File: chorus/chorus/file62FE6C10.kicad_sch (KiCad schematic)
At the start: 7 parts, among them U10 MN3102

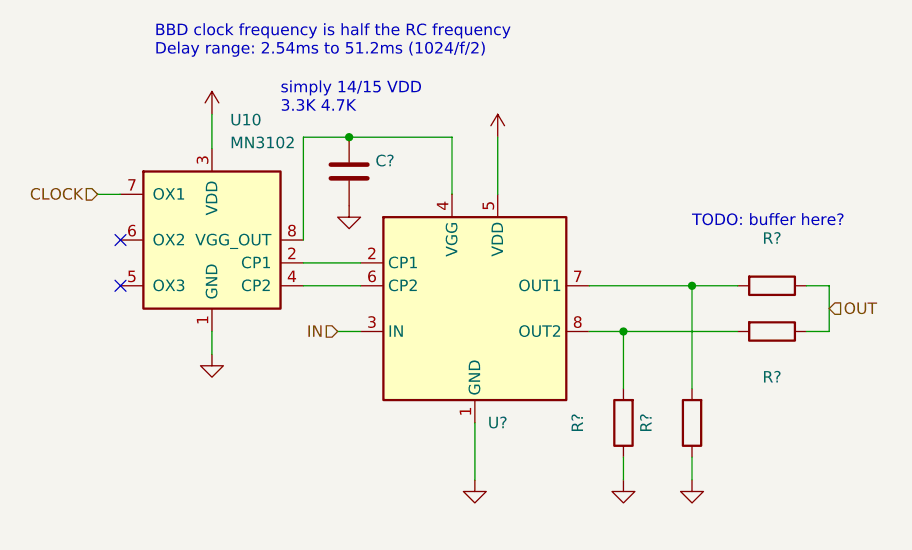
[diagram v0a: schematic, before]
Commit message: add output buffer
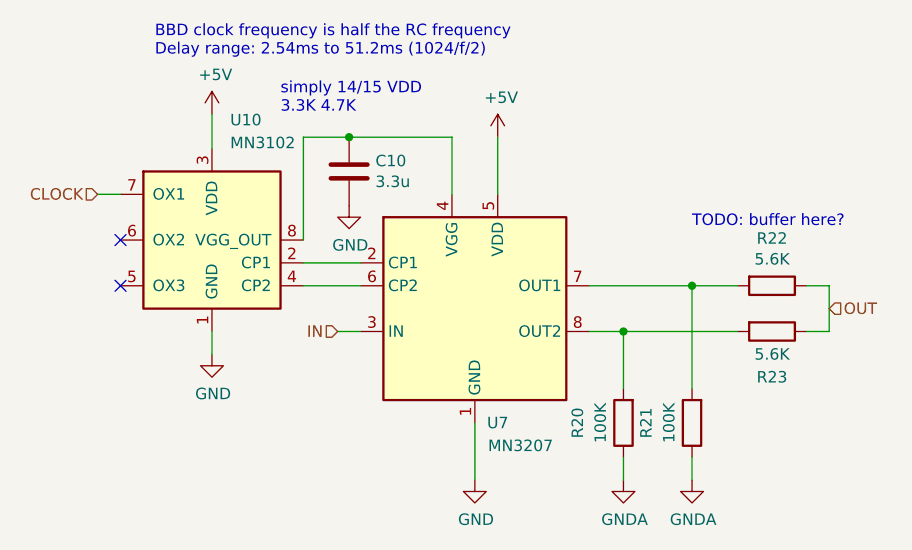
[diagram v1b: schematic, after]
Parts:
- C10: renamed from C?; value (none) -> 3.3u
- R20, R21: renamed from R?; value (none) -> 100K
- R22, R23: renamed from R?; value (none) -> 5.6K
- U7: renamed from U?; value (none) -> MN3207
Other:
- company: (none) -> rabidaudio
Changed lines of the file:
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@@
 (kicad_sch (version 20211123) (generator eeschema)
   (paper "A4")
+  (title_block
+    (company "rabidaudio")
+  )
   (junction (at 167.64 86.36) (diameter 0) (color 0 0 0 0)
   )
@@
   (symbol (lib_id "power:+5V") (at 114.3 67.31 0) (unit 1)
     (in_bom yes) (on_board yes)
-    (property "Reference" "#PWR?" (id 0) (at 114.3 71.12 0)
-      (effects (font (size 1.27 1.27)) hide)
-    )
-    (property "Value" "" (id 1) (at 114.681 62.9158 0))
+    (property "Reference" "#PWR04" (id 0) (at 114.3 71.12 0)
+      (effects (font (size 1.27 1.27)) hide)
+    )
+    (property "Value" "+5V" (id 1) (at 114.681 62.9158 0))
     (property "Footprint" "" (id 2) (at 114.3 67.31 0)
       (effects (font (size 1.27 1.27)) hide)
@@
   (symbol (lib_id "power:+5V") (at 146.05 69.85 0) (unit 1)
     (in_bom yes) (on_board yes)
-    (property "Reference" "#PWR?" (id 0) (at 146.05 73.66 0)
-      (effects (font (size 1.27 1.27)) hide)
-    )
-    (property "Value" "" (id 1) (at 146.431 65.4558 0))
+    (property "Reference" "#PWR05" (id 0) (at 146.05 73.66 0)
+      (effects (font (size 1.27 1.27)) hide)
+    )
+    (property "Value" "+5V" (id 1) (at 146.431 65.4558 0))
     (property "Footprint" "" (id 2) (at 146.05 69.85 0)
       (effects (font (size 1.27 1.27)) hide)
@@
   (symbol (lib_id "Device:R") (at 176.53 91.44 270) (unit 1)
     (in_bom yes) (on_board yes)
-    (property "Reference" "R?" (id 0) (at 176.53 96.52 90))
-    (property "Value" "" (id 1) (at 176.53 93.98 90))
+    (property "Reference" "R23" (id 0) (at 176.53 96.52 90))
+    (property "Value" "5.6K" (id 1) (at 176.53 93.98 90))
     (property "Footprint" "kicad-legacy/kicad-footprints/Resistor_THT.pretty:R_Axial_DIN0204_L3.6mm_D1.6mm_P2.54mm_Vertical" (id 2) (at 176.53 89.662 90)
       (effects (font (size 1.27 1.27)) hide)
@@
   (symbol (lib_id "Device:R") (at 176.53 86.36 270) (unit 1)
     (in_bom yes) (on_board yes)
-    (property "Reference" "R?" (id 0) (at 176.53 81.1022 90))
-    (property "Value" "" (id 1) (at 176.53 83.4136 90))
+    (property "Reference" "R22" (id 0) (at 176.53 81.1022 90))
+    (property "Value" "5.6K" (id 1) (at 176.53 83.4136 90))
     (property "Footprint" "kicad-legacy/kicad-footprints/Resistor_THT.pretty:R_Axial_DIN0204_L3.6mm_D1.6mm_P2.54mm_Vertical" (id 2) (at 176.53 84.582 90)
       (effects (font (size 1.27 1.27)) hide)
@@
   (symbol (lib_id "power:GND") (at 129.54 77.47 0) (unit 1)
     (in_bom yes) (on_board yes)
-    (property "Reference" "#PWR?" (id 0) (at 129.54 83.82 0)
-      (effects (font (size 1.27 1.27)) hide)
-    )
-    (property "Value" "" (id 1) (at 129.667 81.8642 0))
+    (property "Reference" "#PWR0140" (id 0) (at 129.54 83.82 0)
+      (effects (font (size 1.27 1.27)) hide)
+    )
+    (property "Value" "GND" (id 1) (at 129.667 81.8642 0))
     (property "Footprint" "" (id 2) (at 129.54 77.47 0)
       (effects (font (size 1.27 1.27)) hide)
@@
   (symbol (lib_id "Device:C") (at 129.54 73.66 180) (unit 1)
     (in_bom yes) (on_board yes)
-    (property "Reference" "C?" (id 0) (at 132.461 72.4916 0)
+    (property "Reference" "C10" (id 0) (at 132.461 72.4916 0)
       (effects (font (size 1.27 1.27)) (justify right))
     )
-    (property "Value" "" (id 1) (at 132.461 74.803 0)
+    (property "Value" "3.3u" (id 1) (at 132.461 74.803 0)
       (effects (font (size 1.27 1.27)) (justify right))
     )
@@
   (symbol (lib_id "Audio:MN3207") (at 143.51 88.9 0) (unit 1)
     (in_bom yes) (on_board yes)
-    (property "Reference" "U?" (id 0) (at 146.05 101.6 0))
-    (property "Value" "" (id 1) (at 148.59 104.14 0))
+    (property "Reference" "U7" (id 0) (at 146.05 101.6 0))
+    (property "Value" "MN3207" (id 1) (at 148.59 104.14 0))
     (property "Footprint" "kicad-legacy/Housings_DIP.pretty:DIP-8_W7.62mm" (id 2) (at 133.35 81.28 0)
       (effects (font (size 1.27 1.27)) hide)
@@
   (symbol (lib_id "power:GNDA") (at 167.64 107.95 0) (unit 1)
     (in_bom yes) (on_board yes)
-    (property "Reference" "#PWR?" (id 0) (at 167.64 114.3 0)
-      (effects (font (size 1.27 1.27)) hide)
-    )
-    (property "Value" "" (id 1) (at 167.767 112.3442 0))
+    (property "Reference" "#PWR0142" (id 0) (at 167.64 114.3 0)
+      (effects (font (size 1.27 1.27)) hide)
+    )
+    (property "Value" "GNDA" (id 1) (at 167.767 112.3442 0))
     (property "Footprint" "" (id 2) (at 167.64 107.95 0)
       (effects (font (size 1.27 1.27)) hide)
@@
   (symbol (lib_id "power:GNDA") (at 160.02 107.95 0) (unit 1)
     (in_bom yes) (on_board yes)
-    (property "Reference" "#PWR?" (id 0) (at 160.02 114.3 0)
-      (effects (font (size 1.27 1.27)) hide)
-    )
-    (property "Value" "" (id 1) (at 160.147 112.3442 0))
+    (property "Reference" "#PWR0143" (id 0) (at 160.02 114.3 0)
+      (effects (font (size 1.27 1.27)) hide)
+    )
+    (property "Value" "GNDA" (id 1) (at 160.147 112.3442 0))
     (property "Footprint" "" (id 2) (at 160.02 107.95 0)
       (effects (font (size 1.27 1.27)) hide)
@@
   (symbol (lib_id "Device:R") (at 160.02 101.6 180) (unit 1)
     (in_bom yes) (on_board yes)
-    (property "Reference" "R?" (id 0) (at 154.94 101.6 90))
-    (property "Value" "" (id 1) (at 157.48 101.6 90))
+    (property "Reference" "R20" (id 0) (at 154.94 101.6 90))
+    (property "Value" "100K" (id 1) (at 157.48 101.6 90))
     (property "Footprint" "kicad-legacy/kicad-footprints/Resistor_THT.pretty:R_Axial_DIN0204_L3.6mm_D1.6mm_P2.54mm_Vertical" (id 2) (at 161.798 101.6 90)
       (effects (font (size 1.27 1.27)) hide)
@@
   (symbol (lib_id "power:GND") (at 143.51 107.95 0) (unit 1)
     (in_bom yes) (on_board yes)
-    (property "Reference" "#PWR?" (id 0) (at 143.51 114.3 0)
-      (effects (font (size 1.27 1.27)) hide)
-    )
-    (property "Value" "" (id 1) (at 143.637 112.3442 0))
+    (property "Reference" "#PWR0144" (id 0) (at 143.51 114.3 0)
+      (effects (font (size 1.27 1.27)) hide)
+    )
+    (property "Value" "GND" (id 1) (at 143.637 112.3442 0))
     (property "Footprint" "" (id 2) (at 143.51 107.95 0)
       (effects (font (size 1.27 1.27)) hide)
@@
   (symbol (lib_id "Device:R") (at 167.64 101.6 180) (unit 1)
     (in_bom yes) (on_board yes)
-    (property "Reference" "R?" (id 0) (at 162.56 101.6 90))
-    (property "Value" "" (id 1) (at 165.1 101.6 90))
+    (property "Reference" "R21" (id 0) (at 162.56 101.6 90))
+    (property "Value" "100K" (id 1) (at 165.1 101.6 90))
     (property "Footprint" "kicad-legacy/kicad-footprints/Resistor_THT.pretty:R_Axial_DIN0204_L3.6mm_D1.6mm_P2.54mm_Vertical" (id 2) (at 169.418 101.6 90)
       (effects (font (size 1.27 1.27)) hide)
@@
   (symbol (lib_id "power:GND") (at 114.3 93.98 0) (unit 1)
     (in_bom yes) (on_board yes)
-    (property "Reference" "#PWR?" (id 0) (at 114.3 100.33 0)
-      (effects (font (size 1.27 1.27)) hide)
-    )
-    (property "Value" "" (id 1) (at 114.427 98.3742 0))
+    (property "Reference" "#PWR0145" (id 0) (at 114.3 100.33 0)
+      (effects (font (size 1.27 1.27)) hide)
+    )
+    (property "Value" "GND" (id 1) (at 114.427 98.3742 0))
     (property "Footprint" "" (id 2) (at 114.3 93.98 0)
       (effects (font (size 1.27 1.27)) hide)
